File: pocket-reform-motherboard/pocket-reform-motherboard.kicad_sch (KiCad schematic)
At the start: 399 parts, among them J1 CHARGER, J10 1-2199230-6, J11 Conn_01x33, J12 2199230-5, J13 FH35C-31S-0.3HW(50), J14 USB_C_Receptacle, J15 CONN_SPK, J16 SAMTEC_TSM-106-02-X-SH-A, J17 POWSW, J18 CONN_HEAD, J2 DM3AT-SF-PEJM5, J20 QWIIC, J3 USB_C_Receptacle, J4 09452812561, J5 SYSCTL, J6 USB_INT1, J7 HDMI_D_1.4, J8 SIM_Card, J9 Conn_01x20, SW1 SW_DIP_x01, SW2 RESET, SW3 RESET, U1 reform2-som-connector, U10 W25Q32JVSS, U11 PCF8523T, U12 AP22615AWU-7, U13 TXS0108EPW, U14 SN74AVC1T45, U15 TPD4E02B04DQA, U16 TPD4E02B04DQA, U17 TPD12S521, U18 TLV320AIC3100, U19 TPD4E02B04DQA, U2 TS3USB30EDGSR, U20 TPD4E02B04DQA, U21 TPD4E02B04DQA, U22 TPD4E02B04DQA, U23 FUSB302BMPX, U24 TXS0108EPW, U25 TUSB8041, U27 TVS2200DRV, U28 LM62460, U29 TPS62177DQC, U3 LM2830XQMFE/NOPB, U30 TS3USB30EDGSR, U31 TS3USB30EDGSR, U32 AP22615AWU-7, U33 AT24CS02-STUM, U34 PCA9536DP, U35 TMUXHS4446RETR, U36 AP22615AWU-7, U37 TS3USB30EDGSR, U38 CY7C65215-32LTXI, U39 PCA9557RGVR, U4 TLV1117-18, U5 LM73100RPWR, U6 LM62460, U7 74LVC1G34, U8 RP2040, U9 TPS7A0533PDBZ, Y1 24MHz, Y2 12MHz 12pF, Y3 32.768 kHz

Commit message: WIP mb1.5 routing snapshot
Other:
- note added: "TODO: hub power switch"
- note added: "TODO: power switch for PCIe"
- note added: "TODO: wire up clock request"
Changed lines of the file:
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@@
+		)
+	)
+	(text "TODO: hub power switch"
+		(exclude_from_sim no)
+		(at 397.51 439.42 0)
+		(effects
+			(font
+				(size 1.27 1.27)
+			)
 		)
 	)
@@
 		)
 	)
+	(text "TODO: wire up clock request"
+		(exclude_from_sim no)
+		(at 689.61 541.02 0)
+		(effects
+			(font
+				(size 1.27 1.27)
+			)
+		)
+	)
 	(text "Heatsink/SOM Mount"
 		(exclude_from_sim no)
@@
 		(effects
 			(font
+				(size 1.27 1.27)
+			)
+		)
+	)
+	(text "TODO: power switch for PCIe"
+		(exclude_from_sim no)
+		(at 706.12 505.46 0)
+		(effects
+			(font

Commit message: WIP mb20 initial routing complete, and some silkscreen cleanup
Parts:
- removed FB11: 220@100MHz 1.4A, Inductor_SMD:L_0603_1608Metric, symbol Device:FerriteBead_Small
- removed U4: TLV1117-18, Package_TO_SOT_SMD:SOT-223, symbol Regulator_Linear:TLV1117-18
- added R50: 0, Resistor_SMD:R_0402_1005Metric, symbol Device:R_Small
- added U4: TLV75718PDBV, Package_TO_SOT_SMD:SOT-23-5, symbol Regulator_Linear:TLV75718PDBV
- C10, C9: value 1uF -> 4.7uF; LCSC C15849 -> (none); Manufacturer Samsung -> Murata; Manufacturer_No CL10A105KB8NNNC -> GCJ188C70J475KE02D
- J7: footprint Connector_Video:HDMI_Micro-D_Molex_46765-0x01 -> EasyEDA:HDMI-SMD_BX-HDMI-2-M19P; LCSC C585444 -> C18077696; Manufacturer Molex -> Bossie; Manufacturer_No 467650001 -> BX-HDMI-2-M19P
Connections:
- net STANDBY_3V3 is gone; now on net VCC: C13.2, C130.1, C131.1, C135.1, C142.1, C143.1, C144.1, C148.1, C25.1, C27.1, C30.1, C31.1, C32.1, C33.1, C34.1, C35.1, C36.1, C40.1, C46.2, J1.5 (Pin_5), J20.2 (Pin_2), J5.1 (Pin_1), L1.2, R111.2, R113.1, R114.1, R117.2, R127.2, R131.2, R132.1, R133.1, R137.1, R19.2, R38.1, R44.1, R56.1, R57.2, R59.2, R9.2, TP1.1, U10.8 (VCC), U11.8 (VDD), U2.10 (VCC), U23.3 (VDD), U23.4 (VDD), U29.10 (VOS), U30.10 (VCC), U31.10 (VCC), U33.4 (VCC), U34.8 (VDD), U39.14 (VDD), U8.1 (IOVDD), U8.10 (IOVDD), U8.22 (IOVDD), U8.33 (IOVDD), U8.42 (IOVDD), U8.43 (ADC_AVDD), U8.44 (VREG_IN), U8.48 (USB_VDD), U8.49 (IOVDD)
- net +1V1: now also R50.1
- net +1V8: now also U4.5 (OUT)
- net GND: now also J7.20 (SH), U4.2 (GND); no longer J7.SH
- net USBH_1V1: now also R50.2
- net 3V3_1V8: now reaches C9.1, R4.1
- net 3V3_1V8: now also U4.1 (IN), U4.3 (EN)
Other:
- note added: "TODO: more caps!"
- note added: "candidates: - bossie BX-HDMI-2-M19P - megastar ZX-HDMI-WTM19248"
- note removed: "or: ON SEMI NCV1117ST18T3G"
- moved on the sheet: R4

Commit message: WIP mb2.0 polishing
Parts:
- removed C136: 0.1uF, Capacitor_SMD:C_0402_1005Metric, symbol Device:C_Small
- removed C137, C138, C139, C140: 0.22uF, Capacitor_SMD:C_0402_1005Metric, symbol Device:C_Small
- removed FB3, FB4: 100@100MHz 3A, Inductor_SMD:L_0603_1608Metric, symbol pocket-reform-motherboard-rescue:Ferrite_Bead_Small-Device
- removed FB7: 220@100MHz 1.4A, Inductor_SMD:L_0603_1608Metric, symbol Device:FerriteBead_Small
- removed FB8: 100@100MHz 3A, Inductor_SMD:L_0603_1608Metric, symbol Device:FerriteBead_Small
- removed R8: 100k, Resistor_SMD:R_0402_1005Metric, symbol Device:R_Small
- removed U29: TPS62177DQC, Package_SON:WSON-10-1EP_2x3mm_P0.5mm_EP0.84x2.4mm_ThermalVias, symbol Regulator_Switching:TPS62177DQC
- added C109, C150, C151, C154, C155, C156: 0.1uF, Capacitor_SMD:C_0402_1005Metric, symbol Device:C_Small
- added C149, C152, C153: 10uF, Capacitor_SMD:C_0603_1608Metric, symbol Device:C_Small
- added R140: 100k, Resistor_SMD:R_0402_1005Metric, symbol Device:R_Small
- added R141, R144, R145, R156, R159, R160, R162, R163: 10k, Resistor_SMD:R_0402_1005Metric, symbol Device:R_Small
- added R146, R147, R148, R149, R151, R152, R153, R154, R155, R164: 0, Resistor_SMD:R_0402_1005Metric, symbol Device:R_Small
- added R158: 6.8k, Resistor_SMD:R_0402_1005Metric, symbol Device:R_Small
- added R161: 4.7k, Resistor_SMD:R_0402_1005Metric, symbol Device:R_Small
- added R165: 1k, Resistor_SMD:R_0402_1005Metric, symbol Device:R_Small
- added TP10, TP11, TP12, TP13, TP14, TP15, TP16, TP17, TP18, TP19, TP5, TP6: TestPoint, TestPoint:TestPoint_Pad_D1.0mm, symbol Connector:TestPoint
- added U26: TPS542021DDC, Package_TO_SOT_SMD:SOT-23-6, symbol Regulator_Switching:TPS54202DDC
- added U29, U40: AP22615AWU-7, Package_TO_SOT_SMD:SOT-23-6, symbol Regulator_Linear:AP22615AWU
- C133: value 0.1uF -> 10uF; footprint Capacitor_SMD:C_0402_1005Metric -> Capacitor_SMD:C_0603_1608Metric; LCSC (none) -> C92487; Manufacturer Yageo -> Samsung; Manufacturer_No CC0402KRX7R7BB104 -> CL10A106MO8NQNC
- C141, C47: value 0.1uF -> 10uF; footprint Capacitor_SMD:C_0402_1005Metric -> Capacitor_SMD:C_0603_1608Metric; LCSC C1525 -> C92487; Manufacturer_No CL05B104KO5NNNC -> CL10A106MO8NQNC
- C4: value 1uF -> 22uF; footprint Capacitor_SMD:C_0603_1608Metric -> Capacitor_SMD:C_Elec_4x5.4; LCSC (none) -> C3830031; Manufacturer (none) -> Nichicon; Manufacturer_No (none) -> UZG1V4R7MCL1GB
- C58: value 10nF -> 10uF; LCSC C1589 -> C92487; Manufacturer_No CL10B103KB8NNNC -> GRM188R61E106KA73J
- C85, C86, C88, C89, C90, C91, C92, C93: value 0.1uF -> 0.22uF
- FB5, R150, R157: now not fitted
- L3: value 2.7uH -> 3.3uH; LCSC (none) -> C3040366; Manufacturer Pulse -> cijang; Manufacturer_No ??? -> FAUL0650-3R3MT
- L4: LCSC (none) -> C167218; Manufacturer ??? -> cijang; Manufacturer_No ??? -> FXL0630-2R2-M
- R15: value 47k -> 33k
- R7: value 11k -> 124k
- R72: value 10k -> 100k
- R89, R93: value 4.7k -> 2.2k
- R9: value 100k -> 22k; Manufacturer_No RC0402FR-07100KL -> RC0402FR-0710KL
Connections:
- net +1V1: now also TP15.1
- net +1V8: now also TP14.1
- net +3V3: now also C133.1, C58.1, R154.2, R156.2, R160.2, R164.2, TP13.1, U29.6 (IN), U40.6 (IN)
- net +5V: now also TP12.1
- net DP0_N: now also R148.1
- net DP0_P: now also R149.1
- net DP1_N: now also R151.1
- net DP1_P: now also R152.1
- net DP_AUX_N: now also R147.1
- net DP_AUX_P: now also R146.1; no longer C133.1
- net DP_HPD: now also R165.2
- net GND: now also C133.2, R9.2, C149.2, C150.1, C151.2, C152.2, C153.2, C154.1, C155.1, C156.1, R141.2, R144.1, R145.1, R158.2, R159.1, R161.2, R162.1, TP19.1, U26.1 (GND), U29.2 (GND), U40.2 (GND)
- net LPC_MISO: now also TP11.1
- net LPC_MOSI: now also TP5.1
- net LPC_SCK: now also TP10.1
- net LPC_SS0: now also TP6.1
- net MODEM_3V3: now also R164.1
- net SYS_VCC: now also C149.1, C150.2, TP18.1, U26.3 (VIN)
- net USBH_3V3: now also U40.1 (OUT)
- net USBM_DP0_N: now also R148.2
- net USBM_DP0_P: now also R149.2
- net USBM_DP1_N: now also R151.2
- net USBM_DP1_P: now also R152.2
- net USBM_DP_AUX_N: now also R147.2
- net USBM_DP_AUX_P: now also R146.2; no longer C133.2
- net USBM_SBU1: now also J14.A8 (SBU1)
- net USBM_SBU2: now also J14.B8 (SBU2)
- net USB_VBUS: now also TP16.1
- net USB_VBUS2: now also C152.1, C153.1, TP17.1
- net USWITCH_OFF: now also R141.1, R155.1; no longer U39.12 (IO7)
- net VCC: now also C154.2, C155.2, C156.2, R140.1; no longer R9.2
- net ~{STANDBY_SHDN}: now also U26.5 (EN)
- net PCIE_3V3: now reaches C124.1, C126.1, C59.1, C60.1, C61.1, J10.12, J10.14, J10.16, J10.18, J10.2, J10.4, J10.70, J10.72, J10.74, R110.1
- net PCIE_3V3: now also U29.1 (OUT); no longer C58.1
- net at U1.137 (UART4_RXD): now also R153.1
- net at C63.1, C64.1, C65.1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: now also R154.1
- net at U35.14 (A0): now also R144.2
- net at U35.35 (CONF0/A1): now also R145.2
- net at C26.1, C28.1, C29.1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: now also C151.1
- net at U8.36 (GPIO24): now also R165.1
- net PCIE_PWR_EN_L: now reaches U39.11 (IO6)
- net PCIE_PWR_EN_L: now also R159.2, U29.4 (EN)
- net at L1.1: now also C109.1, U26.2 (SW)
- net at R9.1: now also R140.2, U26.4 (FB)
- net at R27.2, U3.5 (Vin): now also R163.1
- net 1V1_ENABLE_L: no longer names the net of U3.4 (EN)
- net 1V1_ENABLE_L: now also R163.2; no longer U39.8 (IO3)
- net M2_CLKREQn renamed PCIE1_CLKREQn
- net PCIE1_CLKREQn: now also R153.2
- new net: R160.1, U40.3 (FLG)
- new net: R161.1, U40.5 (ISET)
- new net: R155.2, U39.12 (IO7)
- new net: R156.1, U29.3 (FLG)
- new net: R158.1, U29.5 (ISET)
- new net: C109.2, U26.6 (BOOT)
- new net HUB_PWR_EN_L: R162.2, U39.8 (IO3), U40.4 (EN)
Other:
- note added: "(note: vqfn and qfn have different pinouts)"
- note added: "4.5V-30V"
- note added: "BRINGUP: adjust ISET"
- note added: "BRINGUP: confirm these new tx caps"
- note added: "BRINGUP: split these signals?"
- note added: "Bossie BX-HDMI-2-M19P"
- note added: "Calculated: OV rising = 22.67V OV falling = 20.78V UV rising = 4.79V UV falling = 4.39V"
- note added: "I2C addresses on RP2040 bus: 0x18: PCA9557 (gpios) 0x22: FUSB302B (usb-c cc) 0x36/0x0b: MAX17320 (prot/monitor) 0x50/0x58: AT24CS02-STUM (eeprom) 0x54: TMUXHS4446 0x5c: MP2650 (charger)"
- note added: "LATER: D5 with less dropout (part selection)"
- note added: "LATER: add DP2+DP3"
- note added: "LATER: any current limiting / monitoring here?"
- note added: "LATER: any termination needed?"
- note added: "LATER: can't turn off 3v3 without resetting"
- note added: "LATER: limit?"
- note added: "LATER: move to sysctl"
- note added: "LATER: pci2 unconnected"
- note added: "LATER: test which of these are required"
- note added: "LATER: unconnected"
- note added: "LATER: wire up clock request on quasar+rk3588"
- note added: "NOTE: Not flipped, use opposite side FPC cable only!"
- note added: "Notes: chip can latch ovlo state. power cycle to reset."
- note added: "SPI test points"
- note added: "TODO: leftover USB pins"
- note added: "downstream of USBH_3V3"
- note added: "has 10k pulldown"
- note added: "has 10k pulldown (active low)"
- note added: "no AC caps here as they are on the device"
- note added: "note: 100k in datasheet"
- note added: "note: changed from 4.7k in V2.0"
- note added: "open drain"
- note added: "unused on V2.0"
- note removed: "4.75-28V"
- note removed: "500mA"
- note removed: "62177 has fixed 3.3V out"
- note removed: "DP from SOM TODO: flip?!"
- note removed: "Not connected"
- note removed: "TODO FIX"
- note removed: "TODO: 0.2uF?"
- note removed: "TODO: 10uF input cap!"
- note removed: "TODO: 10uF/47uF output cap!"
- note removed: "TODO: 3v3 power switch here!"
- note removed: "TODO: C4 cap size"
- note removed: "TODO: HPD to SYSCTL?"
- note removed: "TODO: S/OE matrix"
- note removed: "TODO: add power button"
- note removed: "TODO: address bits"
- note removed: "TODO: any current limiting / monitoring here?"
- note removed: "TODO: any termination needed?"
- note removed: "TODO: bulk cap"
- note removed: "TODO: calc. all resistor values"
- note removed: "TODO: can we bypass latch for disp v2 pwm?"
- note removed: "TODO: clean up choke values mess"
- note removed: "TODO: compare crystal to reference"
- note removed: "TODO: confirm address (conflicts?)"
- note removed: "TODO: confirm this is good, pulls?"
- note removed: "TODO: fix 1uF locations!"
- note removed: "TODO: fix nvme mount position"
- note removed: "TODO: hub power switch"
- note removed: "TODO: leftover"
- note removed: "TODO: limit"
- note removed: "TODO: missing AC caps here to host? double check"
- note removed: "TODO: missing AC caps on TX lines? double check"
- note removed: "TODO: more caps!"
- note removed: "TODO: move status LED to this port"
- note removed: "TODO: move to sysctl"
- note removed: "TODO: power switch for PCIe"
- note removed: "TODO: serial 2 here?"
- note removed: "TODO: sleep pin ??"
- note removed: "TODO: spi test points"
- note removed: "TODO: split these signals?"
- note removed: "TODO: test points for I2C+STANDBY_3V3"
- note removed: "TODO: test points for all power rails"
- note removed: "TODO: test which of these are required"
- note removed: "TODO: unconnected"
- note removed: "TODO: wire up clock request"
- note removed: "candidates: - bossie BX-HDMI-2-M19P - megastar ZX-HDMI-WTM19248"
- note removed: "display enable on V2?"
- note removed: "note: confirm pinout/footprint (tssop vs qfn)"
- moved on the sheet: C132, C135, C145, C2, C38, C5, C75, C80, C84, C94, J17, J20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

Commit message: pocket reform mainboard 2.0 d-1 finished for export
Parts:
- removed U39: PCA9557RGVR, Package_DFN_QFN:Texas_RSA_VQFN-16-1EP_4x4mm_P0.65mm_EP2.7x2.7mm, symbol Interface_Expansion:PCA9557BS
- added U39: PCA9557PW, Package_SO:TSSOP-16_4.4x5mm_P0.65mm, symbol Interface_Expansion:PCA9557PW
- C1, C101, C104, C108, C127, C128, C13, C130, C131, C132, C142, C143, C144, C145, C148, C151, C154, C155, C156, C20, C25, C27, C28, C29, C3, C30, C31, C32, C33, C35, C38, C40, C42, C43, C44, C45, C46, C48, C49, C50, C53, C54, C55, C57, C59, C60, C61, C62, C63, C64, C66, C68, C69, C70, C71, C72, C73, C74, C75, C76, C77, C78, C79, C80, C81, C84, C87, C95, C97, C99: LCSC C1525 -> C307331; Manufacturer_No CL05B104KO5NNNC -> CL05B104KB54PNC
- C10, C9: LCSC (none) -> C437419
- C105, C107, C133, C141, C149, C152, C153, C2, C39, C47, C51, C56, C65, C98: LCSC C92487 -> C194427; Manufacturer Samsung -> muRata; Manufacturer_No CL10A106MO8NQNC -> GRM188R6YA106MA73D
- C109, C121, C150, C19: LCSC C1589 -> C307331; Manufacturer_No CL05B104KO5NNNC -> CL05B104KB54PNC
- C11, C113, C114, C8: LCSC C1589 -> C1623; Manufacturer_No CL10A474KB8NNNC -> CL10B474KA8NNNC
- C110, C122: LCSC C1589 -> C32949; Manufacturer_No GRM1555C1H100FA01D -> CL05C100JB5NNNC
- C111, C125: LCSC C1589 -> C52923; Manufacturer_No CL05A105KO5NNNC -> CL05A105KA5NQNC
- C112, C115, C12, C129, C58, C7: LCSC C92487 -> C194427; Manufacturer Samsung -> muRata; Manufacturer_No GRM188R61E106KA73J -> GRM188R6YA106MA73D
- C116, C117, C118, C119, C120, C14, C15, C16, C17, C18: LCSC C140782 -> C86295; Manufacturer Murata -> Samsung; Manufacturer_No GRM187R61A226ME15D -> CL10A226MP8NUNE
- C135: LCSC C140782 -> C94034; Manufacturer_No GRM188R60J476ME15D -> GRM31CR61A476ME15L
- C146: LCSC (none) -> C162274
- C147: LCSC (none) -> C52923; Manufacturer Taiyo Yuden -> Samsung; Manufacturer_No UMK107BJ105KA-T -> CL05A105KA5NQNC
- C21, C23: LCSC (none) -> C1549; Manufacturer Yageo -> FH; Manufacturer_No (none) -> 0402CG180J500NT
- C26, C36: LCSC C15849 -> C52923; Manufacturer_No CL10A105KB8NNNC -> CL05A105KA5NQNC
- C34: LCSC (none) -> C307331; Manufacturer (none) -> Samsung; Manufacturer_No (none) -> CL05B104KB54PNC
- C37: footprint Capacitor_SMD:C_0603_1608Metric -> Capacitor_SMD:C_0402_1005Metric; LCSC C100040 -> C1523; Manufacturer Yageo -> FH; Manufacturer_No CC0603KRX7R9BB102 -> 0402B102K500NT
- C41: LCSC (none) -> C162274; Manufacturer (none) -> Murata; Manufacturer_No (none) -> GRM188R6YA475KE15D
- C5: LCSC (none) -> C688950; Manufacturer (none) -> Lelon; Manufacturer_No (none) -> VZT470M1HTR-0606
- C96, GFX1, GFX2, H1, H2, H3, H4: now not fitted
- D2: LCSC (none) -> C1847859; Manufacturer_No ESDS314 -> ESDS314DBVR
- D23: value LED_NVME -> LED_RED; LCSC C72044 -> C965799; Manufacturer Everlight -> XINGLIGHT; Manufacturer_No 19-217/R6C-AL1M2VY/3T -> XL-1608SURC-06
- D3: value PMEG1020EA,115 -> MS2A40LWS; LCSC C426863 -> C7380001; Manufacturer Nexperia -> MSKSEMI; Manufacturer_No PMEG1020EA,115 -> MS2A40LWS
- D5: value PMEG4050EP,115 -> PMEG4050EP-FS; LCSC C96235 -> C42387310; Manufacturer Nexperia -> FUXINSEMI; Manufacturer_No PMEG4050EP,115 -> PMEG4050EP-FS
- D8, D9: value LED_Small -> LED_RED; LCSC C72044 -> C965799; Manufacturer Everlight -> XINGLIGHT; Manufacturer_No 19-217/R6C-AL1M2VY/3T -> XL-1608SURC-06
- H5, H7: LCSC (none) -> C18198647
- H8, H9: LCSC (none) -> C22431115
- J10: LCSC Global Sourcing -> C4710843
- J11: LCSC C262220 -> C19077727; Manufacturer Jushuo -> Yuandi; Manufacturer_No AFC07-S33FCC-00 -> FPC-0.5FX-33PH20
- J12: LCSC C590854 -> C4827729
- J13: value FH35C-31S-0.3HW(50) -> 3-2328724-1; LCSC Global Sourcing -> C52722586; Manufacturer TE -> Guoconn; Manufacturer_No 3-2328724-1 -> 0310-31RL-GF-RB
- J15: LCSC (none) -> C177225; Manufacturer_No 53261-7002 -> 532610271
- J16: LCSC (none) -> C6290784
- J17: LCSC (none) -> C160402
- J18: LCSC (none) -> C136657
- J20: LCSC (none) -> C160404
- J4: LCSC DNP -> C19193264
- J9: LCSC (none) -> C2906119; Manufacturer Hirose -> HCTL; Manufacturer_No FH12-20S-0.5SH(55) -> XW05202-200R-00
- L1: LCSC (none) -> C1333678; Manufacturer (none) -> Murata; Manufacturer_No (none) -> DFE322512F-100M=P2
- L5, L6: LCSC C497563 -> C668450; Manufacturer Taiyo Yuden -> Murata; Manufacturer_No NRH3012T150MN -> LQH3NPN150MMEL
- R1, R110, R29, R34, R35, R36, R58, R60, R61: LCSC C106235 -> C11702; Manufacturer Yageo -> UNI-ROYAL; Manufacturer_No RC0402FR-071KL -> 0402WGF1001TCE
- R10, R111, R119, R121, R127, R128, R130, R134, R135, R144, R145, R156, R159, R160, R162, R163, R20, R22, R24, R26, R28, R30, R38, R44, R49, R52, R56, R68, R75, R85, R96: LCSC C60490 -> C25744; Manufacturer Yageo -> UNI-ROYAL; Manufacturer_No RC0402FR-0710KL -> 0402WGF1002TCE
- R100, R73, R97, R98, R99: LCSC C144757 -> C25792; Manufacturer Yageo -> UNI-ROYAL; Manufacturer_No AC0402FR-0747KL -> 0402WGF4702TCE
- R101, R25, R42, R43, R57, R59, R95: LCSC C105871 -> C25900; Manufacturer Yageo -> UNI-ROYAL; Manufacturer_No RC0402FR-074K7L -> 0402WGF4701TCE
- R102: LCSC C163466 -> C25894; Manufacturer Yageo -> UNI-ROYAL; Manufacturer_No RC0402FR-0743K2L -> 0402WGF4322TCE
- R103: LCSC (none) -> C17168; Manufacturer Yageo -> UNI-ROYAL; Manufacturer_No RC0402JR-070RL -> 0402WGF0000TCE
- R104, R105, R106, R107, R108, R109, R11, R116, R118, R12, R122, R123, R124, R13, R133, R139, R146, R147, R148, R149, R151, R152, R153, R154, R155, R164, R19, R27, R33, R4, R46, R5, R50, R53, R54, R62, R65, R66, R67, R81: LCSC C242160 -> C17168; Manufacturer Panasonic -> UNI-ROYAL; Manufacturer_No ERJ2GE0R00X -> 0402WGF0000TCE
- R112, R51, R69, R70, R87: LCSC C60491 -> C25741; Manufacturer Yageo -> UNI-ROYAL; Manufacturer_No RC0402FR-07100KL -> 0402WGF1003TCE
- R113, R114, R115, R117, R131, R141: LCSC C242160 -> C25744; Manufacturer Yageo -> UNI-ROYAL; Manufacturer_No RC0402JR-0710KL -> 0402WGF1002TCE
- R120, R161: LCSC (none) -> C25900; Manufacturer (none) -> UNI-ROYAL; Manufacturer_No (none) -> 0402WGF4701TCE
- R125, R94: LCSC C60491 -> C25744; Manufacturer Yageo -> UNI-ROYAL; Manufacturer_No RC0402JR-0710KL -> 0402WGF1002TCE
- R126, R92: LCSC C60490 -> C25903; Manufacturer Yageo -> UNI-ROYAL; Manufacturer_No RC0402FR-074K99L -> 0402WGF4991TCE
- R129, R158, R32: LCSC (none) -> C17772; Manufacturer (none) -> UNI-ROYAL; Manufacturer_No (none) -> 0805W8F6801T5E
- R132, R137: Manufacturer Yageo -> UNI-ROYAL; Manufacturer_No RC0402FR-072K2L -> 0402WGF2201TCE
- R136: LCSC (none) -> C17168; Manufacturer Vishay Dale -> UNI-ROYAL; Manufacturer_No CRCW06030000Z0EAC -> 0402WGF0000TCE
- R138: LCSC C242160 -> C25744; Manufacturer Panasonic -> UNI-ROYAL; Manufacturer_No ERJ2GE0R00X -> 0402WGF1002TCE
- R140, R72: LCSC C60490 -> C25741; Manufacturer Yageo -> UNI-ROYAL; Manufacturer_No RC0402FR-0710KL -> 0402WGF1003TCE
- R15: LCSC (none) -> C25779; Manufacturer (none) -> UNI-ROYAL; Manufacturer_No (none) -> 0402WGF3302TCE
- R150, R157: LCSC (none) -> C25741; Manufacturer Yageo -> UNI-ROYAL; Manufacturer_No RC0402FR-07100KL -> 0402WGF1003TCE
- R16: LCSC (none) -> C11702; Manufacturer (none) -> UNI-ROYAL; Manufacturer_No (none) -> 0402WGF1001TCE
- R165, R45: LCSC C242160 -> C11702; Manufacturer Panasonic -> UNI-ROYAL; Manufacturer_No ERJ2GE0R00X -> 0402WGF1001TCE
- R17, R91: LCSC C60490 -> C25741; Manufacturer Yageo -> UNI-ROYAL; Manufacturer_No RC0402FR-07100KL -> 0402WGF1003TCE
- R18: LCSC C163466 -> C25874; Manufacturer Yageo -> UNI-ROYAL; Manufacturer_No RC0402FR-0724K9L -> 0402WGF2492TCE
- R198, R199: LCSC C87044 -> C25120; Manufacturer Yageo -> UNI-ROYAL; Manufacturer_No RC0402FR-0749R9L -> 0402WGF499JTCE
- R2: LCSC C144787 -> C26083; Manufacturer Yageo -> UNI-ROYAL; Manufacturer_No AC0402FR-071ML -> 0402WGF1004TCE
- R23: LCSC C321660 -> C96273; Manufacturer FH -> UNI-ROYAL; Manufacturer_No RC-02W9531FT -> 0402WGF9531TCE
- R31: LCSC (none) -> C21189; Manufacturer (none) -> UNI-ROYAL; Manufacturer_No (none) -> 0603WAF0000T5E
- R37, R39, R40, R41: LCSC C413061 -> C25133; Manufacturer Panasonic -> UNI-ROYAL; Manufacturer_No ERJ2RKF75R0X -> 0402WGF750JTCE
- R55, R86: LCSC DNP -> C25105; Manufacturer Yageo -> UNI-ROYAL; Manufacturer_No RC0402FR-0733RL -> 0402WGF330JTCE; now not fitted
- R6: LCSC (none) -> C25790; Manufacturer (none) -> UNI-ROYAL; Manufacturer_No (none) -> 0402WGF4703TCE
- R63: LCSC C60491 -> C11702; Manufacturer Yageo -> UNI-ROYAL; Manufacturer_No RC0402FR-071KL -> 0402WGF1001TCE
- R64: LCSC C114762 -> C25879; Manufacturer Yageo -> UNI-ROYAL; Manufacturer_No RC0402FR-072K2L -> 0402WGF2201TCE
- R7: LCSC (none) -> C36777; Manufacturer (none) -> UNI-ROYAL; Manufacturer_No (none) -> 0402WGF1243TCE
- R71: LCSC C60491 -> C11702; Manufacturer Yageo -> UNI-ROYAL; Manufacturer_No AC0402DR-071KL -> 0402WGF1001TCE
- R76, R77, R79, R80, R82: LCSC C138002 -> C25105; Manufacturer Yageo -> UNI-ROYAL; Manufacturer_No RC0402FR-0733RL -> 0402WGF330JTCE
- R83, R84: LCSC C144778 -> C25768; Manufacturer Yageo -> UNI-ROYAL; Manufacturer_No AC0402FR-0722KL -> 0402WGF2202TCE
- R89, R93: LCSC C105871 -> C25879; Manufacturer Yageo -> UNI-ROYAL; Manufacturer_No RC0402FR-074K7L -> 0402WGF2201TCE
- R9: LCSC C60490 -> C25768; Manufacturer Yageo -> UNI-ROYAL; Manufacturer_No RC0402FR-0710KL -> 0402WGF2202TCE
- R90: LCSC C413101 -> C25771; Manufacturer Panasonic -> UNI-ROYAL; Manufacturer_No ERJ2RKF2702X -> 0402WGF2702TCE
- SW1: LCSC C402914 -> C3312106; Manufacturer Dongguan Guangzhu -> Nidec; Manufacturer_No DSIC01LSGET -> CHS-01A1
- TP1, TP10, TP11, TP12, TP13, TP14, TP15, TP16, TP17, TP18, TP19, TP2, TP3, TP4, TP5, TP6: Manufacturer (none) -> DNP; Manufacturer_No (none) -> DNP; now not fitted
- U1: LCSC (none) -> C590722; Manufacturer_No 1473149-1 -> 1717254-1
- U12, U29, U32, U36, U40: Manufacturer (none) -> Diodes; Manufacturer_No (none) -> AP22615AWU-7
- U2, U30, U31, U37: LCSC (none) -> C131998
- U25: LCSC (none) -> C544686; Manufacturer_No TUSB8041 -> TUSB8041IRGCR
- U26: LCSC (none) -> C44811646; Manufacturer (none) -> Texas Instruments; Manufacturer_No (none) -> TPS542021DDC
- U27: LCSC (none) -> C523793
- U28, U6: LCSC (none) -> C3198091
- U33: LCSC (none) -> C2060969; Manufacturer (none) -> Microchip; Manufacturer_No (none) -> AT24CS02-STUM-T
- U34: LCSC (none) -> C14674; Manufacturer NXP -> Texas Instruments; Manufacturer_No PCA9536DP,118 -> PCA9536DGKR
- U35: LCSC (none) -> C35471229; Manufacturer (none) -> Texas Instruments; Manufacturer_No (none) -> TMUXHS4446RETR
- U38: LCSC (none) -> C22451897
- U4: LCSC (none) -> C507270
- U5: LCSC (none) -> C3210761; Manufacturer (none) -> Texas Instruments; Manufacturer_No (none) -> LM73100RPWR
- U7: LCSC C7394031 -> C353880
- U9: LCSC (none) -> C2877921
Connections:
- net 3V3_ENABLE_L: now also U39.9 (IO2)
- net 5V_ENABLE_L: now also U39.7 (IO1)
- net DISP_BL_PWR_EN_L: now also U39.12 (IO5)
- net GND: now also U39.4 (A1), U39.5 (A2), U39.8 (VSS)
- net HUB_PWR_EN_L: now also U39.10 (IO3)
- net PCIE_PWR_EN_L: now also U39.13 (IO6)
- net RP_SCL0: now also U39.1 (SCL)
- net RP_SDA0: now also U39.2 (SDA)
- net VCC: now also U39.16 (VDD)
- net ~{DISP_RESET_L}: now also U39.11 (IO4)
- net at R137.2: now also U39.15 (~{RESET})
- net at R132.2: now also U39.3 (A0)
- net at R155.2: now also U39.14 (IO7)
- net at R46.1: now also U39.6 (IO0)
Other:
- note added: "compat: TI PCA9536DGKR"

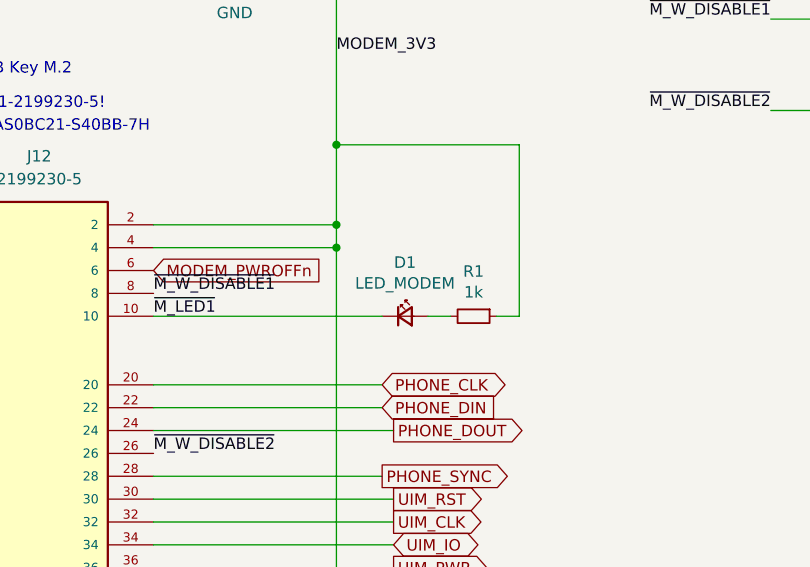
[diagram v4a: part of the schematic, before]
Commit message: pocket reform mainboard 2.0 d-1 BOM fixes during sample order
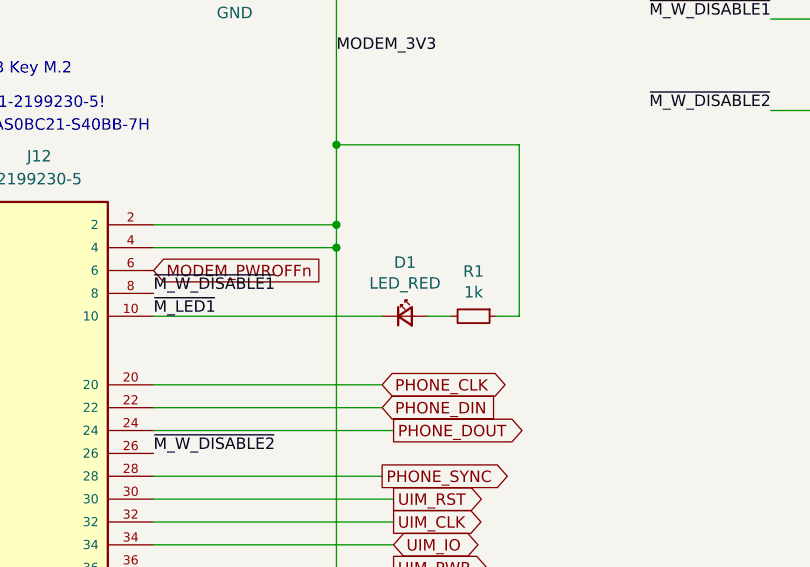
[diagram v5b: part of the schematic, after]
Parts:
- C106, C67: LCSC C86295 -> C45783; Manufacturer_No CL10A226MP8NUNE -> CL21A226MAQNNNE
- C146, C41: LCSC C162274 -> C23733; Manufacturer Murata -> Samsung; Manufacturer_No GRM188R6YA475KE15D -> CL05A475MP5NRNC
- D1: value LED_MODEM -> LED_RED; LCSC C72044 -> C965799; Manufacturer Everlight -> XINGLIGHT; Manufacturer_No 19-217/R6C-AL1M2VY/3T -> XL-1608SURC-06
- R129, R158, R32: LCSC C17772 -> C25917; Manufacturer_No 0805W8F6801T5E -> 0402WGF6801TCE
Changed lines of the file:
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@@
 			)
 		)
-		(property "Value" "LED_MODEM"
+		(property "Value" "LED_RED"
 			(at 787.4 378.6124 0)
 			(effects
@@
 			)
 		)
-		(property "Manufacturer" "Everlight"
+		(property "Manufacturer" "XINGLIGHT"
 			(at 787.4 382.27 0)
 			(effects
@@
 			)
 		)
-		(property "Manufacturer_No" "19-217/R6C-AL1M2VY/3T"
+		(property "Manufacturer_No" "XL-1608SURC-06"
 			(at 787.4 382.27 0)
 			(effects
@@
 			)
 		)
-		(property "LCSC" "C72044"
+		(property "LCSC" "C965799"
 			(at 787.4 382.27 0)
 			(effects
@@
 			)
 		)
-		(property "LCSC" "C17772"
+		(property "LCSC" "C25917"
 			(at 751.84 114.3 0)
 			(effects
@@
 			)
 		)
-		(property "Manufacturer_No" "0805W8F6801T5E"
+		(property "Manufacturer_No" "0402WGF6801TCE"
 			(at 751.84 114.3 0)
 			(effects
@@
 			)
 		)
-		(property "Manufacturer_No" "GRM188R6YA475KE15D"
+		(property "Manufacturer_No" "CL05A475MP5NRNC"
 			(at 621.03 -92.71 0)
 			(effects
@@
 			)
 		)
-		(property "Manufacturer" "Murata"
+		(property "Manufacturer" "Samsung"
 			(at 621.03 -92.71 0)
 			(effects
@@
 			)
 		)
-		(property "LCSC" "C162274"
+		(property "LCSC" "C23733"
 			(at 621.03 -92.71 0)
 			(effects
@@
 			)
 		)
-		(property "Manufacturer_No" "CL10A226MP8NUNE"
+		(property "Manufacturer_No" "CL21A226MAQNNNE"
 			(at 1007.11 668.02 0)
 			(effects
@@
 			)
 		)
-		(property "LCSC" "C86295"
+		(property "LCSC" "C45783"
 			(at 1007.11 668.02 0)
 			(effects
@@
 			)
 		)
-		(property "Manufacturer" "Murata"
+		(property "Manufacturer" "Samsung"
 			(at 751.84 228.6 0)
 			(effects
@@
 			)
 		)
-		(property "Manufacturer_No" "GRM188R6YA475KE15D"
+		(property "Manufacturer_No" "CL05A475MP5NRNC"
 			(at 751.84 228.6 0)
 			(effects
@@
 			)
 		)
-		(property "LCSC" "C162274"
+		(property "LCSC" "C23733"
 			(at 751.84 228.6 0)
 			(effects
@@
 			)
 		)
-		(property "LCSC" "C17772"
+		(property "LCSC" "C25917"
 			(at 692.15 535.94 0)
 			(effects
@@
 			)
 		)
-		(property "Manufacturer_No" "0805W8F6801T5E"
+		(property "Manufacturer_No" "0402WGF6801TCE"
 			(at 692.15 535.94 0)
 			(effects
@@
 			)
 		)
-		(property "LCSC" "C17772"
+		(property "LCSC" "C25917"
 			(at 867.41 110.49 0)
 			(effects
@@
 			)
 		)
-		(property "Manufacturer_No" "0805W8F6801T5E"
+		(property "Manufacturer_No" "0402WGF6801TCE"
 			(at 867.41 110.49 0)
 			(effects
@@
 			)
 		)
-		(property "Manufacturer_No" "CL10A226MP8NUNE"
+		(property "Manufacturer_No" "CL21A226MAQNNNE"
 			(at 1007.11 648.97 0)
 			(effects
@@
 			)
 		)
-		(property "LCSC" "C86295"
+		(property "LCSC" "C45783"
 			(at 1007.11 648.97 0)
 			(effects
